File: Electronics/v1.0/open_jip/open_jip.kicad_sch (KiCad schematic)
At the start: 22 parts

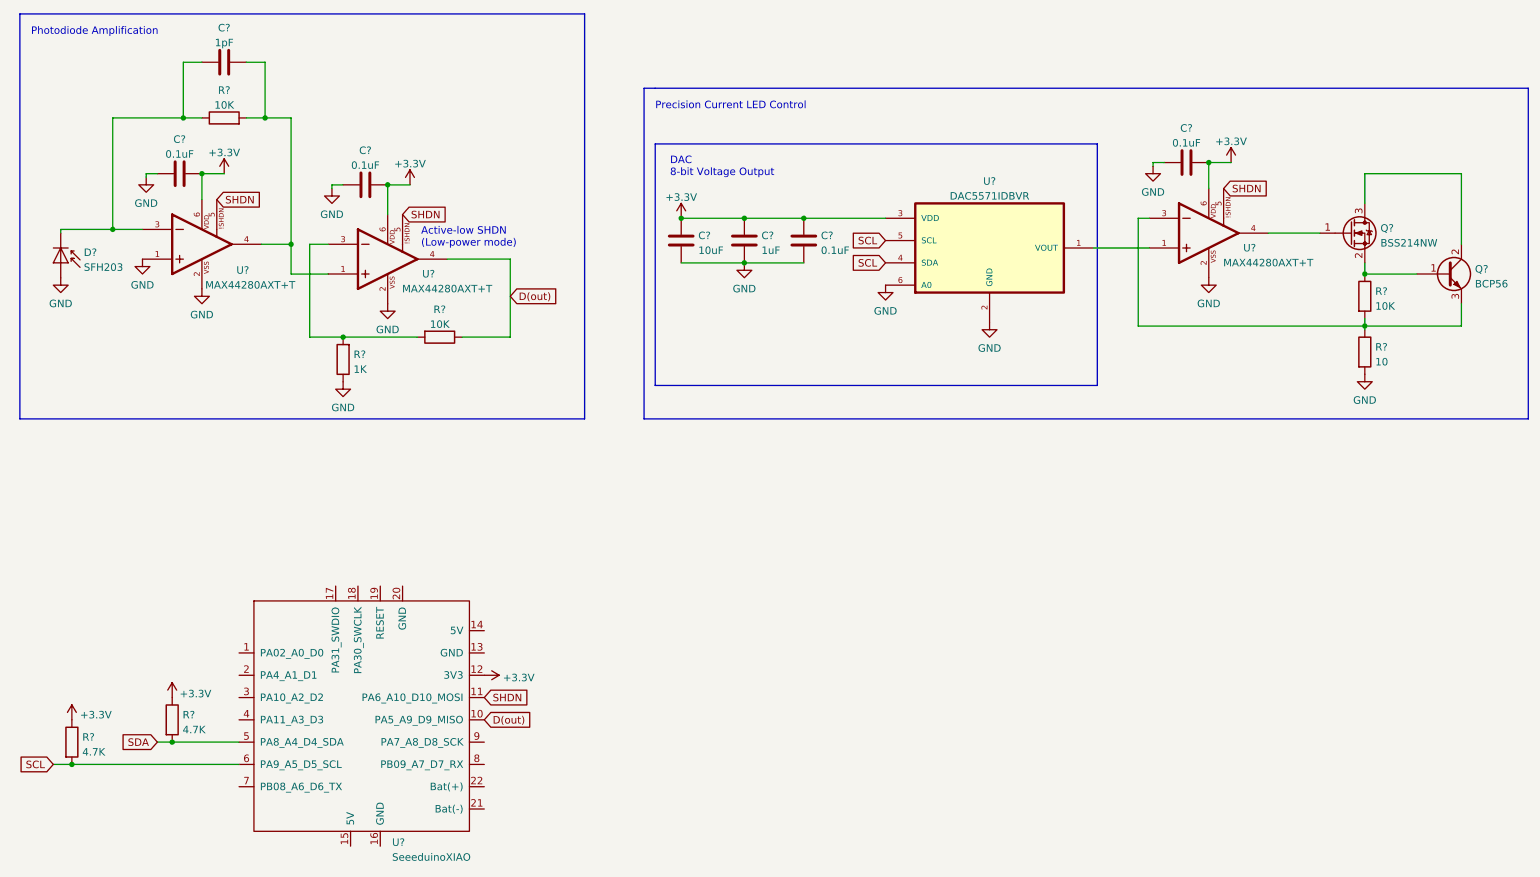
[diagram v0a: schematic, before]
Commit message: added precision current source for excitation LED
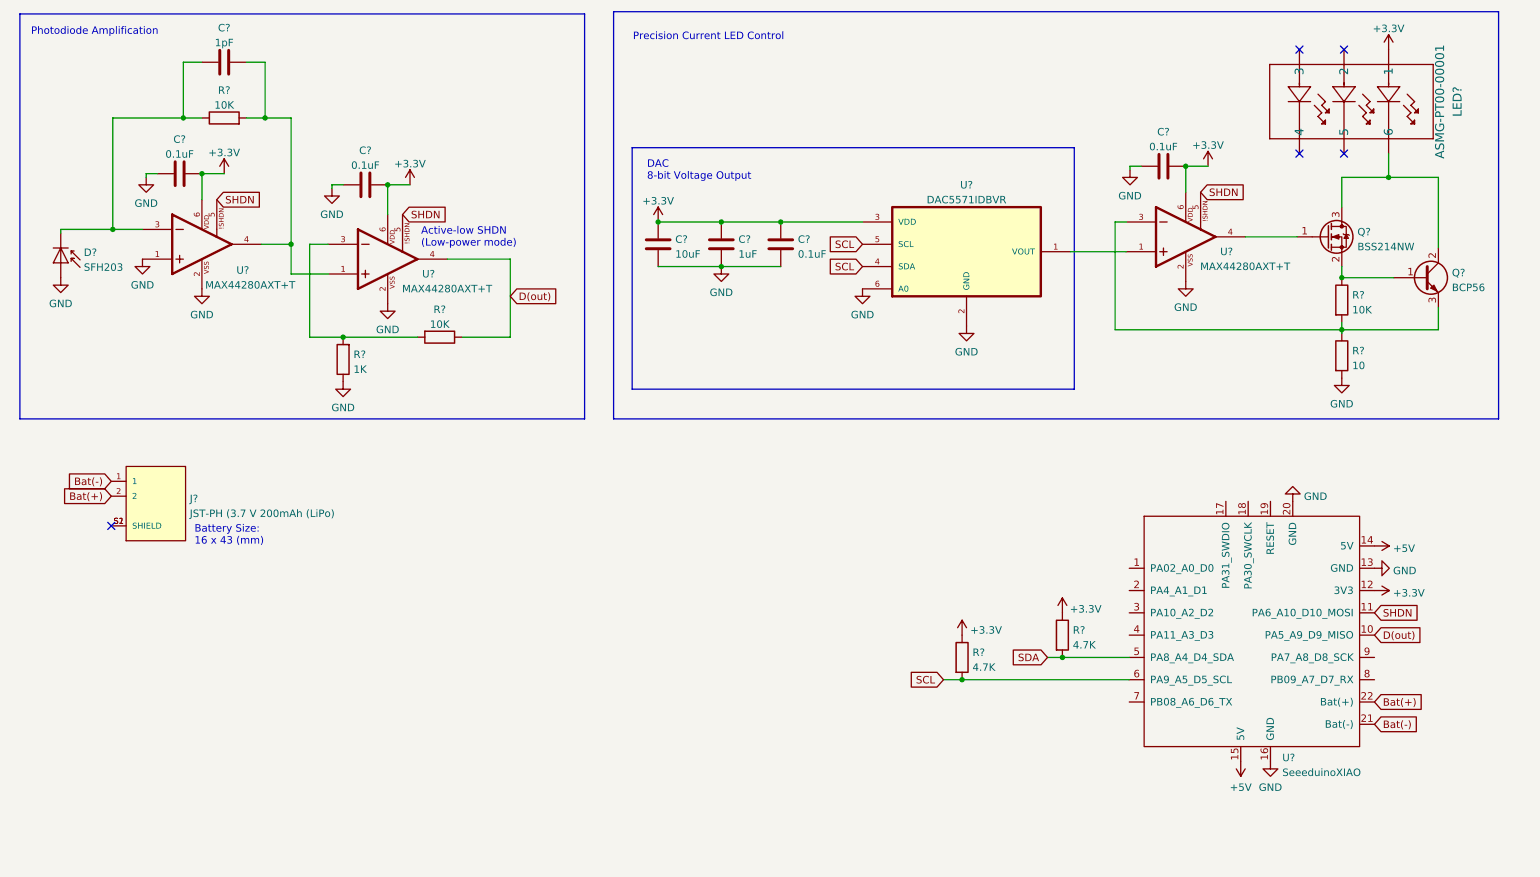
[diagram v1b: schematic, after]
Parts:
- added J?: JST-PH (3.7 V 200mAh (LiPo), JST_S2B-PH-SM4-TB(LF)(SN), symbol S2B-PH-SM4-TB_LF__SN_:S2B-PH-SM4-TB(LF)(SN)
- added LED?: ASMG-PT00-00001, ASMG-PT00_BRA, symbol ASMG-PT00-00001:ASMG-PT00-00001
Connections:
- net +3.3V: now also LED?.1
- net GND: now also U?.13 (GND), U?.16 (GND), U?.20 (GND)
- net at Q?.2 (C), Q?.3 (D), Q?.4 (C): now also LED?.6
- net +5V: now reaches U?.14 (5V)
- net +5V: now also U?.15 (5V)
- net Bat(-): now reaches U?.21 (Bat(-))
- net Bat(-): now also J?.1
- net Bat(+): now reaches U?.22 (Bat(+))
- net Bat(+): now also J?.2
- new net: J?.S1 (SHIELD), J?.S2 (SHIELD)
- no-connect marks 0 -> 5
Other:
- note added: "Battery Size: 16 x 43 (mm)"
- moved on the sheet: C?, Q?, R?, U?

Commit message: finalised prototype components and started on PCB
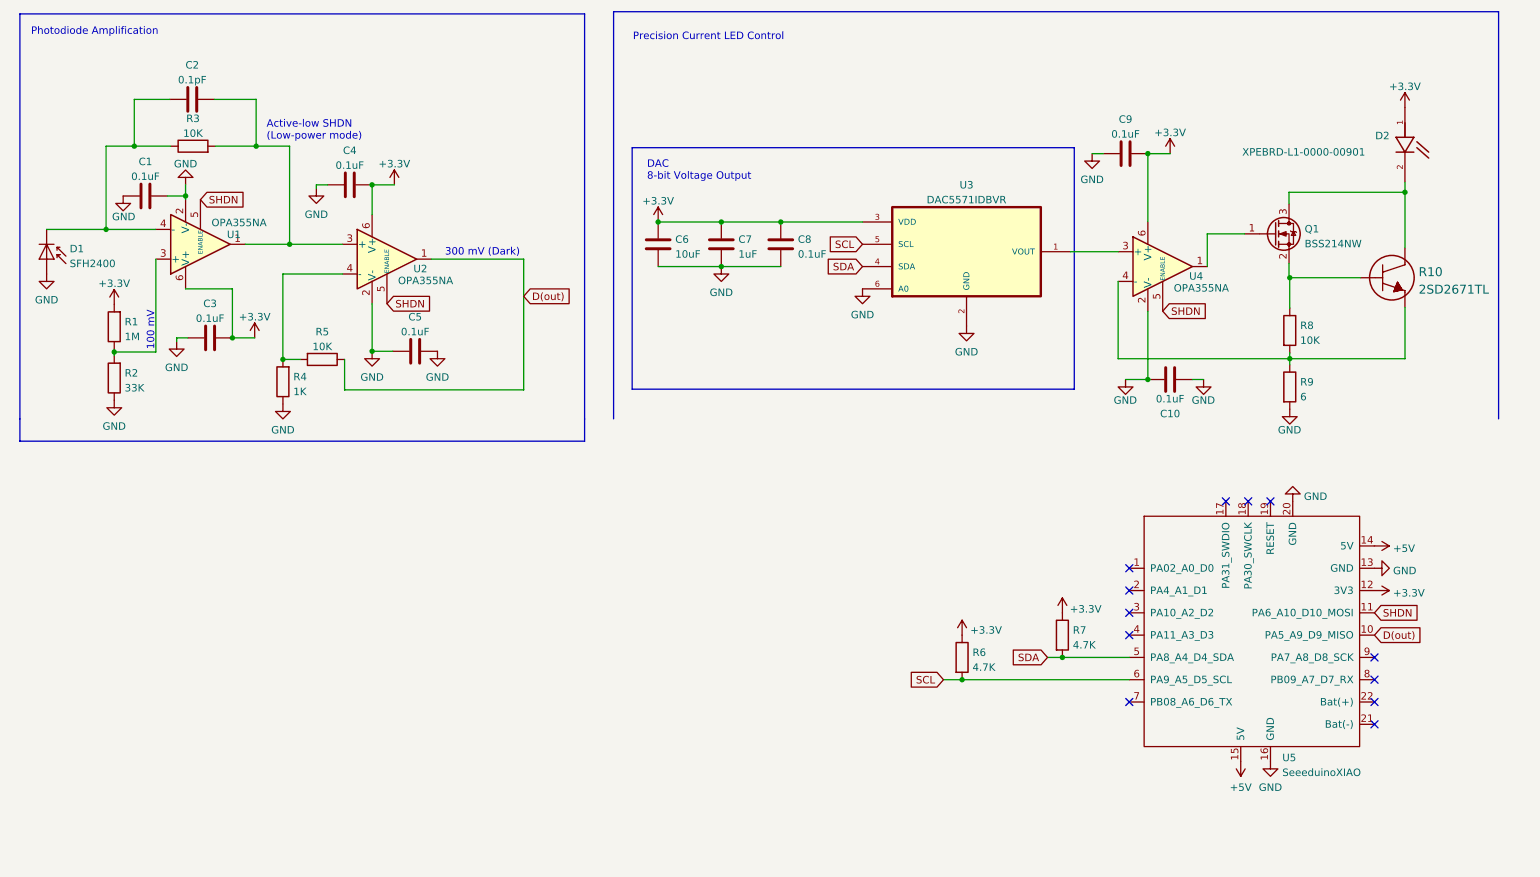
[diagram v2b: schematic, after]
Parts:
- removed D?: SFH203, LED_THT:LED_D5.0mm_IRGrey, symbol Sensor_Optical:SFH203
- removed J?: JST-PH (3.7 V 200mAh (LiPo), JST_S2B-PH-SM4-TB(LF)(SN), symbol S2B-PH-SM4-TB_LF__SN_:S2B-PH-SM4-TB(LF)(SN)
- removed LED?: ASMG-PT00-00001, ASMG-PT00_BRA, symbol ASMG-PT00-00001:ASMG-PT00-00001
- removed Q?: BSS214NW, Package_TO_SOT_SMD:SOT-323_SC-70, symbol Transistor_FET:BSS214NW
- removed Q?: BCP56, Package_TO_SOT_SMD:SOT-223-3_TabPin2, symbol Transistor_BJT:BCP56
- removed R?: 10, symbol Device:R
- removed R?: 10K, symbol Device:R
- removed U? (x3): MAX44280AXT+T, SOP65P220X110-6N, symbol MAX44280AXT_T:MAX44280AXT+T
- added C1, C10, C5: 0.1uF, Capacitor_SMD:C_0805_2012Metric, symbol Device:C
- added D1: SFH2400, OptoDevice:Osram_SMD-SmartDIL, symbol Sensor_Optical:SFH2400
- added D2: XPEBRD-L1-0000-00901, XPEBRD-L1-0000-00901:LED_XPEBRD-L1-0000-00901, symbol XPEBRD-L1-0000-00901:XPEBRD-L1-0000-00901
- added Q1: BSS214NW, Package_TO_SOT_SMD:SOT-323_SC-70, symbol Transistor_FET:BSS214NW
- added R1: 1M, Resistor_SMD:R_0805_2012Metric, symbol Device:R
- added R10: 2SD2671TL, 2SD2671TL:2SD2671TL, symbol 2SD2671TL:2SD2671TL
- added R2: 33K, Resistor_SMD:R_0805_2012Metric, symbol Device:R
- added R8: 10K, Resistor_SMD:R_0805_2012Metric, symbol Device:R
- added R9: 6, Resistor_SMD:R_2512_6332Metric, symbol Device:R
- added U1, U2, U4: OPA355NA, Package_TO_SOT_SMD:SOT-23-6, symbol Amplifier_Operational:OPA355NA
- C2: renamed from C?; value 1pF -> 0.1pF; footprint (none) -> Capacitor_SMD:C_0805_2012Metric
- C3, C4, C6, C7, C8, C9: renamed from C?; footprint (none) -> Capacitor_SMD:C_0805_2012Metric
- R3, R4, R5, R6, R7: renamed from R?; footprint (none) -> Resistor_SMD:R_0805_2012Metric
- U3: renamed from U?; footprint SOT95P280X145-6N -> DAC5571IDBVR:SOT95P280X145-6N
- U5: renamed from U?; footprint (none) -> Seeeduino XIAO:Seeeduino XIAO-MOUDLE14P-2.54-21X17.8MM
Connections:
- net +3.3V: now also D2.1, R1.2, U1.6 (V+), U2.6 (V+), U4.6 (V+)
- net D(out): now also U2.1
- net GND: now also C1.1, C1.2, C10.1, C10.2, C5.1, C5.2, D1.2 (A), R2.1, R9.2, U1.2 (V-), U2.2 (V-), U4.2 (V-)
- net SCL: no longer U3.4 (SDA)
- net SDA: now also U3.4 (SDA)
- net SHDN: now also U1.5 (ENABLE), U2.5 (ENABLE), U4.5 (ENABLE)
- net at U3.1 (VOUT): now also U4.3 (+)
- net at C2.2, R3.2: now also U1.1, U2.3 (+)
- net at R4.2, R5.2: now also U2.4 (-)
- net at C2.1, R3.1: now also D1.1 (K), U1.4 (-)
- net Bat(+): no longer names the net of U5.22 (Bat(+))
- net Bat(-): no longer names the net of U5.21 (Bat(-))
- new net: R1.1, R2.2, U1.3 (+)
- new net: D2.2, Q1.3 (D), R10.1
- new net: Q1.2 (S), R10.2, R8.1
- new net: R10.3, R8.2, R9.1, U4.4 (-)
- new net: Q1.1 (G), U4.1
- no-connect marks 5 -> 12
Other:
- note added: "100 mV"
- note added: "300 mV (Dark)"
- note removed: "Battery Size: 16 x 43 (mm)"
- moved on the sheet: C2, C3, C4, C9, R3, R4, R5

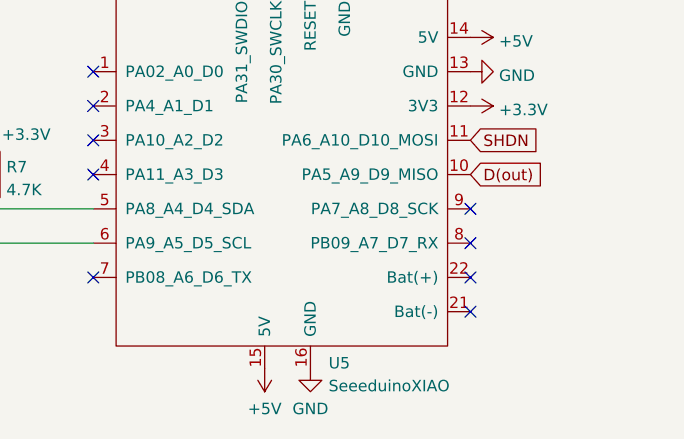
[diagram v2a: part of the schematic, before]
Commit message: updated file structure of project
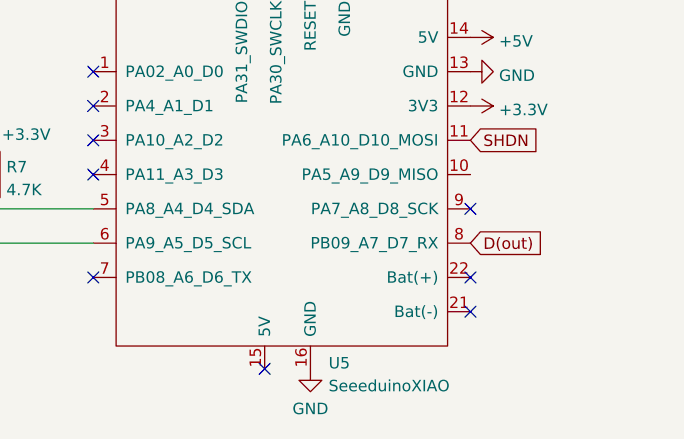
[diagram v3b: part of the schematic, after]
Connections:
- net +5V: no longer U5.15 (5V)
- net D(out): now also U5.8 (PB09_A7_D7_RX); no longer U5.10 (PA5_A9_D9_MISO)
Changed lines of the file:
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@@
   (no_connect (at 255.016 140.462))
   (no_connect (at 255.016 129.032))
-  (no_connect (at 255.016 132.842))
   (no_connect (at 229.616 102.362))
   (no_connect (at 233.426 102.362))
   (no_connect (at 237.236 102.362))
+  (no_connect (at 232.156 146.812))
   (wire (pts (xy 132.588 54.61) (xy 143.383 54.61))
     (stroke (width 0) (type default) (color 0 0 0 0))
@@
     )
   )
-  (global_label "D(out)" (shape input) (at 255.016 125.222 0) (fields_autoplaced)
+  (global_label "D(out)" (shape input) (at 255.016 132.842 0) (fields_autoplaced)
     (effects (font (size 1.27 1.27)) (justify left))
-    (property "Intersheet References" "${INTERSHEET_REFS}" (id 0) (at 263.3273 125.1426 0)
+    (property "Intersheet References" "${INTERSHEET_REFS}" (id 0) (at 263.3273 132.7626 0)
       (effects (font (size 1.27 1.27)) (justify left) hide)
     )
@@
     )
     (property "Datasheet" "" (id 3) (at 184.531 125.222 0)
-      (effects (font (size 1.27 1.27)) hide)
-    )
-    (pin "1")
-  )
-  (symbol (lib_id "power:+5V") (at 232.156 146.812 180) (unit 1)
-    (in_bom yes) (on_board yes) (fields_autoplaced)
-    (property "Reference" "#PWR0116" (id 0) (at 232.156 143.002 0)
-      (effects (font (size 1.27 1.27)) hide)
-    )
-    (property "Value" "+5V" (id 1) (at 232.156 151.2554 0))
-    (property "Footprint" "" (id 2) (at 232.156 146.812 0)
-      (effects (font (size 1.27 1.27)) hide)
-    )
-    (property "Datasheet" "" (id 3) (at 232.156 146.812 0)
       (effects (font (size 1.27 1.27)) hide)
     )
@@
       (reference "#PWR0115") (unit 1) (value "+3.3V") (footprint "")
     )
-    (path "/a1dbe802-9133-4d60-9cd0-fedd23881dc0"
-      (reference "#PWR0116") (unit 1) (value "+5V") (footprint "")
-    )
     (path "/82161823-27c8-4e1e-9191-90c14340bd8f"
